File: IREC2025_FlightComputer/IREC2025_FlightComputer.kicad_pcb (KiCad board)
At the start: 2 copper layers, 149 parts, among them J1 Molex Microfit, Q1 SI7232DN-T1-GE3, Q2 SI7232DN-T1-GE3, U1 STM32U575VGTx, U10 PE4259-63, U11 SX1262IMLTRT, U12 ADXL375BCCZ-RL7, U13 MMC5983MA, U14 BMI088, U15 TMP275AIDGKR VSSOP8, U16 MS5607-02BA, U17 KLM4G1FETE-B041, U18 SAM-M10Q-00B, U2 NRVB120VLSFT1G, U4 NRVB120VLSFT1G, U5 LP5912Q3.3DRVRQ1, U8 TPS62153, U9 SN74HCT125DR, X1 1XXD32000MBA, X2 1XXD32000MBA

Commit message: Updated 22/3/2025
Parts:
- added C22: 100nF, PCM_JLCPCB:C_0402, F.Cu at (145.9, 123.5)
- added J2: BOOT0, Connector_PinHeader_2.54mm:PinHeader_1x03_P2.54mm_Vertical, F.Cu at (96.3, 105.8)
- added J3: SWD, Connector_PinHeader_2.54mm:PinHeader_1x04_P2.54mm_Vertical, F.Cu at (142.2, 124.9)
- added R9: 10kΩ, PCM_JLCPCB:R_0402, F.Cu at (145.9, 126.5)
- moved D2 40.2 mm to (131.9, 87.4)
- moved C23 39.7 mm to (124.6, 111.0)
- moved U8 33.1 mm to (126.8, 87.9)
- moved X1 31.6 mm to (131.5, 108.6)
- moved FB1 31.2 mm to (132.5, 99.8)
- moved L1 31.2 mm to (132.5, 102.6)
- moved R8 21.7 mm to (131.8, 76.7)
- moved C20 21.7 mm to (131.6, 79.3)
- moved D4 21.7 mm to (131.9, 73.7)
- moved C27 21.5 mm to (132.4, 105.5)
- moved U4 21.4 mm to (101.4, 107.9)
- moved U2 21.4 mm to (101.4, 104.9)
- moved D3 21.2 mm to (127.7, 83.2)
- moved U14 20.2 mm to (132.5, 119.8)
- moved R20 20.2 mm to (124.0, 117.9)
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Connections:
- U1 pad 12: unconnected-(U1-PH0-Pad12) -> HSE_IN
- U1 pad 14: NRST -> /NRST
- U1 pad 70: unconnected-(U1-PA11-Pad70) -> USB_DN
- U1 pad 71: MS5607_CS -> USB_DP
- U1 pad 72: unconnected-(U1-PA13-Pad72) -> SWDIO
- U1 pad 76: unconnected-(U1-PA14-Pad76) -> SWCLK
- U1 pad 77: unconnected-(U1-PA15-Pad77) -> MS5607_NSS
- U1 pad 81: BMI_accel_INT1 -> BMI_GYRO_CS
- U1 pad 82: BMI_GYRO_INT1 -> BMI_accel_CS
- U1 pad 83: unconnected-(U1-PD2-Pad83) -> BMI_accel_INT1
- U1 pad 84: unconnected-(U1-PD3-Pad84) -> BMI_GYRO_INT1
- U1 pad 94: unconnected-(U1-PH3-Pad94) -> /BOOT0
- U16 pad 4: MS5607_CS -> MS5607_NSS
- U16 pad 5: MS5607_CS -> MS5607_NSS
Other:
- copper layers 2 -> 4

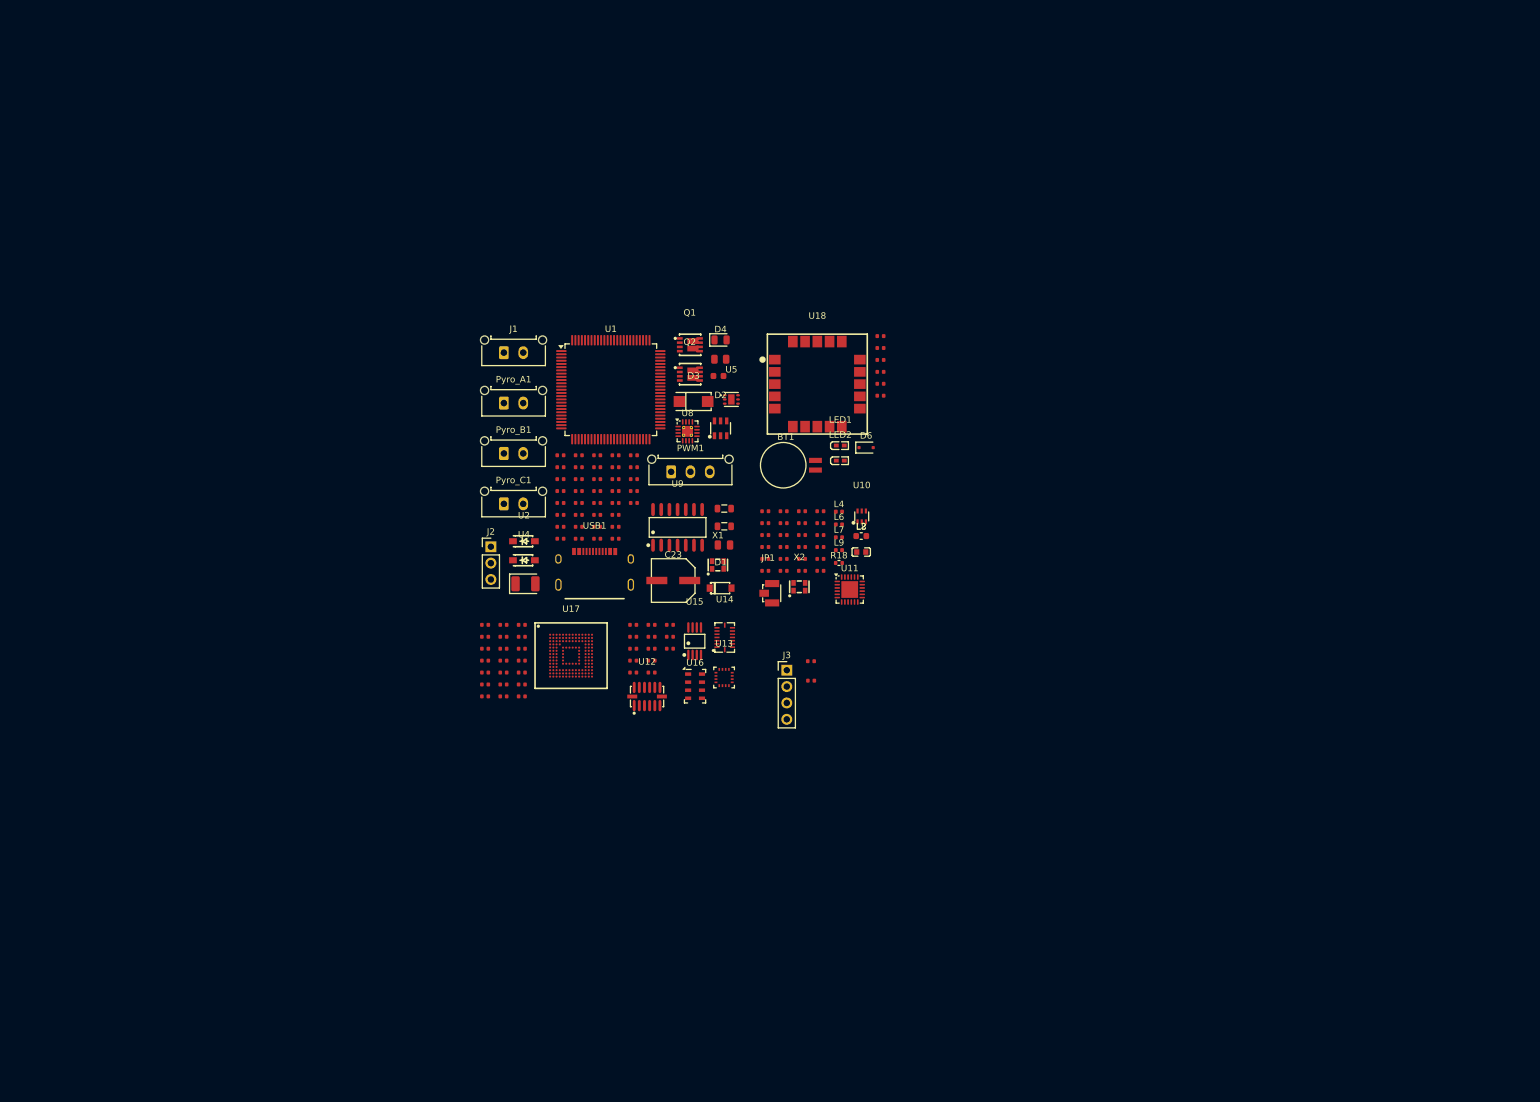
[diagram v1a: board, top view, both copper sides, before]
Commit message: Updated schematic + initiate layout
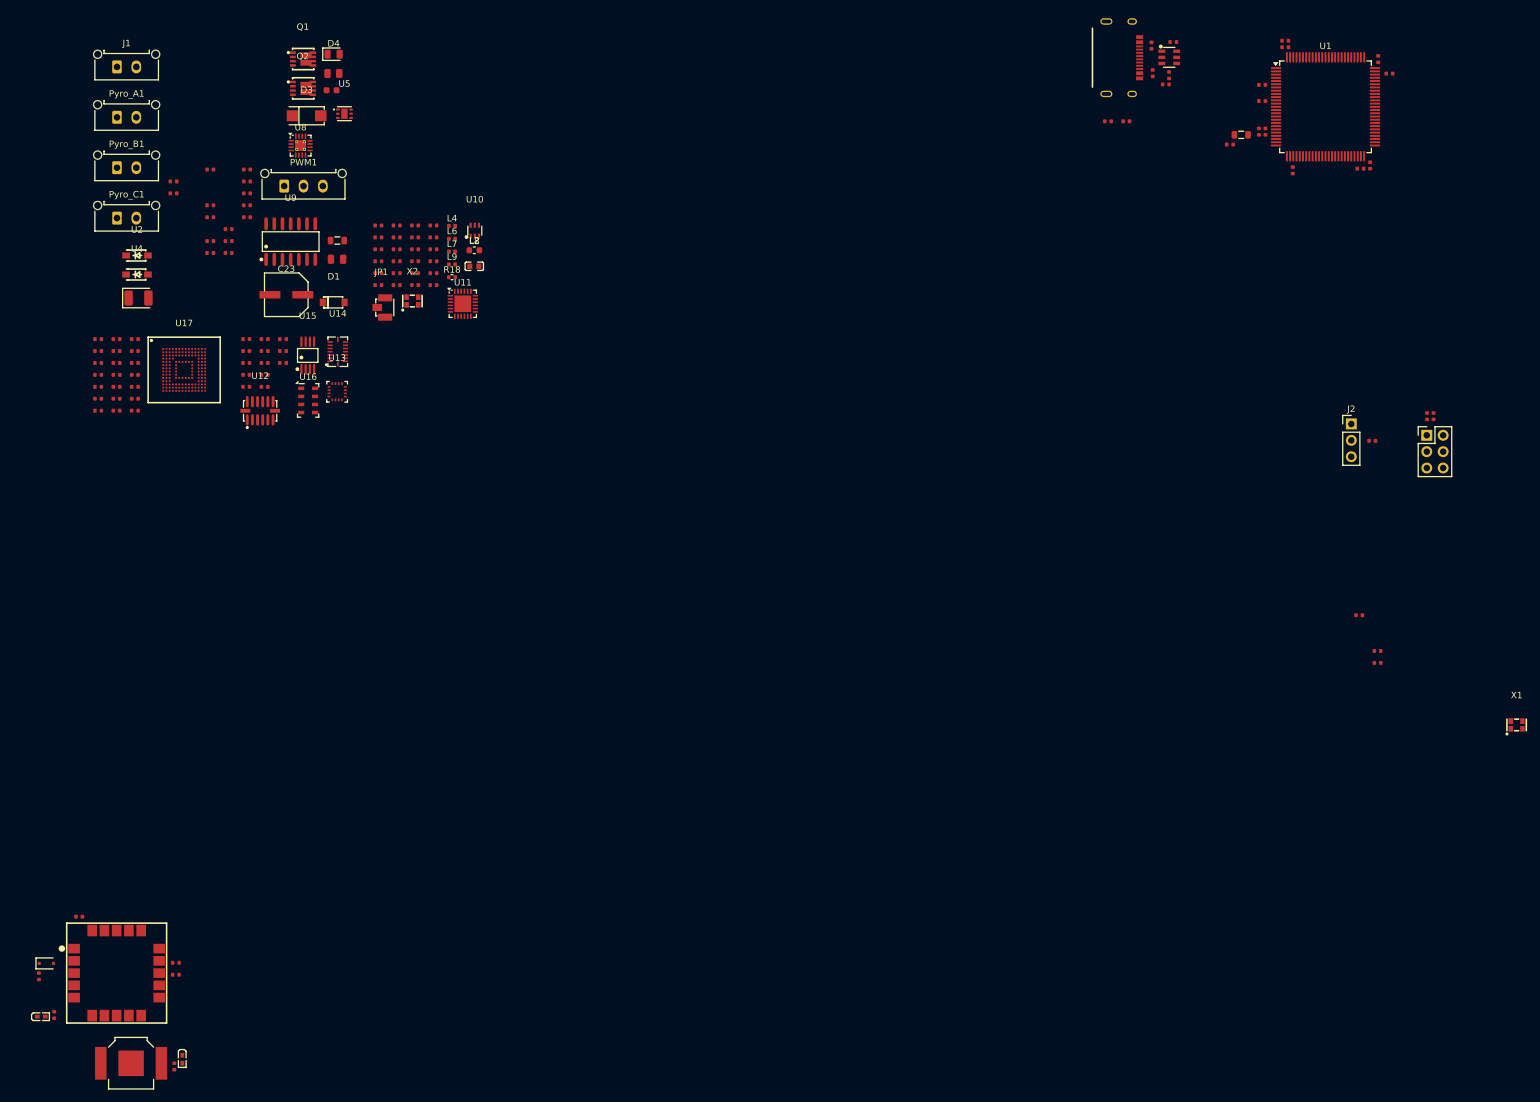
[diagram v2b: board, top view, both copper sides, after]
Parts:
- removed J3: SWD, Connector_PinHeader_2.54mm:PinHeader_1x04_P2.54mm_Vertical
- added J4: Conn_02x03_Counter_Clockwise, Connector_PinHeader_2.54mm:PinHeader_2x03_P2.54mm_Vertical, F.Cu at (241.5, 88.5)
- added R38: 10kΩ, PCM_JLCPCB:R_0402, F.Cu at (241.5, 85.5)
- BT1: value Battery -> 3098; footprint Battery:BatteryHolder_Seiko_MS621F -> GNSS:BAT_3098
- moved R35 162.4 mm to (28.5, 178.4), turned to -90 degrees
- moved R37 158.6 mm to (26.1, 172.4), turned to -90 degrees
- moved C71 153.5 mm to (32.4, 163.2)
- moved R36 152.4 mm to (47.1, 186.4), turned to -90 degrees
- moved LED1 152.4 mm to (26.5, 178.7)
- moved D6 150.3 mm to (27.3, 170.4)
- moved C8 147.5 mm to (235.7, 32.4)
- moved C6 145.2 mm to (233.9, 30.1), turned to 90 degrees
- moved R33 145.1 mm to (47.4, 170.3)
- moved R34 145.1 mm to (47.4, 172.2)
- moved U18 142.0 mm to (38.2, 171.9)
- moved BT1 141.0 mm to (40.4, 185.9)
- moved LED2 138.0 mm to (48.4, 185.3), turned to -90 degrees
- moved C5 136.1 mm to (232.7, 46.6), turned to -90 degrees
- moved C7 134.8 mm to (219.5, 28.2)
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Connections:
- net /BOOT0 renamed Net-(U1-PH3)
- net /NRST renamed nRST
- net Net-(J2-Pin_2) renamed BOOT0
- C14 pad 1: Net-(C14-Pad1) -> +3.3VA
- C15 pad 1: Net-(C14-Pad1) -> +3.3VA
- C16 pad 1: +3.3VA -> +3.3V
- D2 pad 1: D- -> D+
- D2 pad 3: USB_DN -> D-
- D2 pad 4: USB_DP -> USB_DN
- D2 pad 6: D+ -> USB_DP
- FB1 pad 1: Net-(C14-Pad1) -> +3.3VA
- FB1 pad 2: +3.3VA -> +3.3V
- R36 pad 1: +3V3 -> Net-(LED2-+)
- R36 pad 2: Net-(LED2-+) -> Backup
- U1 pad 16: unconnected-(U1-PC1-Pad16) -> eMMC_CLK
- U1 pad 33: unconnected-(U1-PC4-Pad33) -> COMPANION_TX
- U1 pad 34: unconnected-(U1-PC5-Pad34) -> COMPANION_RX
- U1 pad 51: ADXL_NSS -> unconnected-(U1-PB12-Pad51)
- U1 pad 52: ADXL_SCLK -> unconnected-(U1-PB13-Pad52)
- U1 pad 53: ADXL_MISO -> DAT1
- U1 pad 54: ADXL_MOSI -> DAT0
- U1 pad 63: unconnected-(U1-PC6-Pad63) -> DAT7
- U1 pad 64: unconnected-(U1-PC7-Pad64) -> DAT6
- U1 pad 88: unconnected-(U1-PD7-Pad88) -> eMMC_CMD
- U1 pad 89: unconnected-(U1-PB3-Pad89) -> DAT2
- U1 pad 90: unconnected-(U1-PB4-Pad90) -> DAT3
- U1 pad 95: unconnected-(U1-PB8-Pad95) -> DAT4
- U1 pad 96: unconnected-(U1-PB9-Pad96) -> DAT5

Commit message: update idk
25/3/2025
starting to take shape (i guess)
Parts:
- C57, C58, C59, R19, R20, R21, R22: moved to B.Cu
- D3: footprint EasyEDA:SMA_L4.4-W2.6-LS5.0-RD -> GNSS:DIOM7959X262N
- L1: footprint PCM_JLCPCB:L_0805 -> EasyEDA:IND-SMD_L4.0-W4.0_XFL4020-102MEB
- moved R2 152.5 mm to (203.6, 38.2)
- moved C17 151.1 mm to (203.6, 39.4)
- moved C55 150.0 mm to (207.3, 63.6)
- moved C54 149.3 mm to (207.2, 68.5)
- moved C25 148.9 mm to (200.8, 38.7)
- moved U2 148.1 mm to (188.6, 44.1)
- moved R1 147.9 mm to (199.0, 36.9)
- moved R10 146.0 mm to (201.0, 43.4), turned to 90 degrees
- moved R19 143.9 mm to (204.3, 66.1), turned to 90 degrees
- moved C59 143.6 mm to (202.1, 51.8), turned to 90 degrees
- moved J1 143.5 mm to (181.7, 32.6), turned to 180 degrees
- moved U4 142.5 mm to (182.6, 44.1), turned to 180 degrees
- moved R20 141.9 mm to (205.8, 69.0), turned to 90 degrees
- moved C57 139.0 mm to (197.9, 50.9)
- moved C58 138.7 mm to (198.2, 55.9), turned to -90 degrees
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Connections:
- U1 pad 33: COMPANION_TX -> COMPANION_RX
- U1 pad 34: COMPANION_RX -> COMPANION_TX
- U1 pad 59: unconnected-(U1-PD12-Pad59) -> MMC_SCL
- U1 pad 60: unconnected-(U1-PD13-Pad60) -> MMC_SDA
- U1 pad 78: SPI3_SCLK -> BMI_SCLK
- U1 pad 79: SPI3_MISO -> BMI_MISO
- U1 pad 80: SPI3_MOSI -> BMI_MOSI
- U1 pad 82: BMI_accel_CS -> unconnected-(U1-PD1-Pad82)
- U1 pad 83: BMI_accel_INT1 -> unconnected-(U1-PD2-Pad83)
- U1 pad 85: unconnected-(U1-PD4-Pad85) -> BMI_GYRO_INT2
- U1 pad 86: unconnected-(U1-PD5-Pad86) -> BMI_accel_CS
- U1 pad 87: unconnected-(U1-PD6-Pad87) -> BMI_accel_INT1
- U1 pad 92: unconnected-(U1-PB6-Pad92) -> TMP_SCL
- U1 pad 93: unconnected-(U1-PB7-Pad93) -> TMP_SDA
- U12 pad 1: VBAT- -> +3.3V
- U16 pad 6: MS5607_MISO -> BMI_MISO
- U16 pad 7: MS5607_MOSI -> BMI_MOSI
- U16 pad 8: MS5607_SCLK -> BMI_SCLK
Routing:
- net BMI_MISO: track 0.00 -> 18.5 mm, vias 0 -> 3
- net BMI_SCLK: track 0.00 -> 11.6 mm
- net BMI_accel_INT1: track 0.00 -> 5.97 mm
- net BMI_accel_CS: track 0.00 -> 4.94 mm
- net BMI_GYRO_INT2: track 0.00 -> 4.94 mm
- net BMI_GYRO_INT1: track 0.00 -> 4.94 mm
- net BMI_MOSI: track 0.00 -> 4.73 mm
- net TMP_SCL: track 0.00 -> 3.57 mm, vias 0 -> 1
- net TMP_SDA: track 0.00 -> 3.54 mm, vias 0 -> 1
- net MS5607_NSS: track 0.00 -> 2.15 mm
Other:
- board text added: "ADXL"
- board text added: "GNSS"

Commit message: checkpoint
before the great layout change
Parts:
- removed C19: 100nF, PCM_JLCPCB:C_0402
- removed C29: 3.0pF, PCM_JLCPCB:C_0402
- removed C33, C36, C40, C42: C_Small, PCM_JLCPCB:C_0402
- removed C44: 1uF, PCM_JLCPCB:C_0402
- removed C62, C63, C64, C65, C66, C67, C68, C69: 10nF, PCM_JLCPCB:C_0402
- removed D4: 3v3_led, LED_SMD:LED_0805_2012Metric
- removed JP1: U.FL-R-SMT-1(10), EasyEDA:ANT-SMD_UFL-R-SMT-1-10
- removed L8: 15nH, Inductor_SMD:L_0603_1608Metric
- removed Pyro_C1: Molex Microfit, Connector_Molex:Molex_Micro-Fit_3.0_43650-0215_1x02_P3.00mm_Vertical
- removed Q2: SI7232DN-T1-GE3, EasyEDA:POWER-1212-8_L3.3-W3.3-P0.66-LS3.3-BL
- removed R18: 1k, Resistor_SMD:R_0402_1005Metric
- removed R25, R26, R27, R28, R29, R30, R32, R7: 22kΩ, PCM_JLCPCB:R_0402
- removed R31: 47kΩ, PCM_JLCPCB:R_0402
- removed R5: 1MΩ, PCM_JLCPCB:R_0402
- removed R6: 10kΩ, PCM_JLCPCB:R_0402
- removed R8: 1kΩ, PCM_JLCPCB:R_0805
- removed U17: KLM4G1FETE-B041, EasyEDA:FBGA-153_L11.0-W10.0-P0.50_KLM4G1FETE-B041
- added BZ1: PKMCS0909E4000-R1, Buzzer_Beeper:PUIAudio_SMT_0825_S_4_R, F.Cu at (84.7, 91.5)
- added C24: 10uF, PCM_JLCPCB:C_0805, F.Cu at (90.4, 138.6)
- added C73: 10uF, PCM_JLCPCB:C_0402, F.Cu at (72.4, 95.2)
- added C74: 100uF, EasyEDA:CAP-SMD_L3.2-W1.6, F.Cu at (107.1, 123.2)
- added H1: MountingHole_Pad, MountingHole:MountingHole_3.2mm_M3_DIN965_Pad, F.Cu at (120.9, 139.0)
- added H2: MountingHole_Pad, MountingHole:MountingHole_3.2mm_M3_DIN965_Pad, F.Cu at (54.6, 139.2)
- added H3: MountingHole_Pad, MountingHole:MountingHole_3.2mm_M3_DIN965_Pad, F.Cu at (141.3, 54.2)
- added H4: MountingHole_Pad, MountingHole:MountingHole_3.2mm_M3_DIN965_Pad, F.Cu at (33.3, 62.9)
- added LOGO: LOGO, Cuharlogo:CUHARLOGOMOD, F.Cu at (29.5, 88.6)
- added R49: 22kΩ, PCM_JLCPCB:R_0402, B.Cu at (97.2, 113.3)
- added R50: 22kΩ, PCM_JLCPCB:R_0402, B.Cu at (93.8, 105.0)
- added R51: 22kΩ, PCM_JLCPCB:R_0402, F.Cu at (84.7, 102.3)
- added R52: 22kΩ, PCM_JLCPCB:R_0402, B.Cu at (96.0, 102.7)
- added R53: 22kΩ, PCM_JLCPCB:R_0402, F.Cu at (81.1, 102.9)
- added R54: 22kΩ, PCM_JLCPCB:R_0402, F.Cu at (78.5, 105.9)
- added R55: 22kΩ, PCM_JLCPCB:R_0402, F.Cu at (76.0, 102.3)
- added R56: 22kΩ, PCM_JLCPCB:R_0402, F.Cu at (76.0, 105.7)
- added R57: 22kΩ, PCM_JLCPCB:R_0402, F.Cu at (69.7, 95.6)
- added R58: 47kΩ, PCM_JLCPCB:R_0402, F.Cu at (71.2, 109.8)
- added RF1: SMA-KE-5, EasyEDA:SMA-TH_SMA-KHDB_C9900020423, F.Cu at (61.9, 71.3)
- added SERVO2: Conn_01x03_Pin, Connector_Molex:Molex_Micro-Fit_3.0_43650-0315_1x03_P3.00mm_Vertical, F.Cu at (55.6, 121.0)
- added U6: ~, RFshielddd:MS233-20, F.Cu at (79.1, 69.9)
- added U7: THGBMUG6C1LBAIL, EasyEDA:BGA-153_L13.0-W11.5-P0.50-TL_KLM8G1GEME-B041, F.Cu at (67.5, 101.6)
- C11, C34, C35, C43, C45, C51, C52, C53, R9: moved to B.Cu
- C20: footprint PCM_JLCPCB:C_0603 -> PCM_JLCPCB:C_0805; moved to B.Cu
- C21: footprint PCM_JLCPCB:C_0402 -> PCM_JLCPCB:C_0603
- C23: value RVT1E101M0607 -> 22uF; footprint EasyEDA:CAP-SMD_BD6.3-L6.6-W6.6-LS7.2-R-RD -> PCM_JLCPCB:C_0603; moved to B.Cu
- C25: value 3.3pF -> GJM1555C1H3R3BB01D; footprint PCM_JLCPCB:C_0402 -> EasyEDA:C0402
- C26: footprint PCM_JLCPCB:C_0402 -> PCM_JLCPCB:C_0603; moved to B.Cu
- C27: value 22uF -> GJM1555C1H390JB01D; footprint PCM_JLCPCB:C_0805 -> PCM_JLCPCB:C_0402
- C28: footprint PCM_JLCPCB:C_CASE-B-3528-21(mm) -> EasyEDA:CAP-SMD_L3.2-W1.6
- C37: value C_Small -> 3pF
- C38: value C_Small -> 5.6pF
- C39: value C_Small -> 2.4pF
- C4: footprint PCM_JLCPCB:C_0402 -> PCM_JLCPCB:C_0805
- C41: value 10nF -> 39pF
- C46, C47: value C_Small -> GJM1555C1H3R3BB01D; footprint PCM_JLCPCB:C_0402 -> EasyEDA:C0402
- C48: value C_Small -> GRM155R72A102KA01D; footprint PCM_JLCPCB:C_0402 -> EasyEDA:C0402
- C49: value 10nF -> 1uF; moved to B.Cu
- C50: value 1nF -> GRM155R72A102KA01D; footprint PCM_JLCPCB:C_0402 -> EasyEDA:C0402
- C60: value 10uF -> 1.8pF
- C61: value 10nF -> 1.8pF
- C70: value 10uF -> 100nF
- L3: value 47nH -> 15uH; footprint PCM_JLCPCB:C_0402 -> EasyEDA:L0805; moved to B.Cu
- L4: value 0R -> 47nH; footprint Inductor_SMD:L_0402_1005Metric -> PCM_JLCPCB:L_0402
- L6: value L_Small -> 4.7nH
- L7: value L_Small -> 15nH
- L9: value L_Small -> LQW15AN9N1H00D
- R11: value 3.3kΩ -> 0R
- R23, R24: value 22kΩ -> CRCW0402100RFKED
- moved BT1 159.1 mm to (108.6, 42.1), turned to 180 degrees
- moved R36 154.8 mm to (101.9, 41.6), turned to 90 degrees
- moved LED2 151.8 mm to (100.7, 42.7), turned to 90 degrees
- moved R2 150.9 mm to (87.0, 134.0), turned to 180 degrees
- moved C17 149.3 mm to (87.0, 132.7), turned to 180 degrees
- moved X1 147.8 mm to (109.8, 107.9), turned to 180 degrees
- moved D1 147.7 mm to (85.9, 130.4), turned to 0 degrees
- moved C25 145.7 mm to (90.0, 133.4)
- moved R1 145.3 mm to (91.6, 134.7), turned to 180 degrees
- moved R37 145.3 mm to (104.2, 49.9), turned to 180 degrees
- moved D6 143.1 mm to (106.2, 51.0), turned to -90 degrees
- moved D3 141.4 mm to (98.4, 137.7), turned to 0 degrees
- moved R10 140.4 mm to (89.5, 128.6), turned to -90 degrees
- moved U8 138.3 mm to (93.5, 131.8), turned to -90 degrees
- moved LED1 137.4 mm to (94.1, 59.0), turned to 180 degrees
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- renumbered Pyro_A1 to Pyro_CH1, Pyro_B1 to Pyro_CH2, PWM1 to SERVO1
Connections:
- C23 pad 1: Net-(U2-K) -> VBAT-
- C23 pad 2: VBAT- -> +5V
- C25 pad 1: Net-(U8-SS/TR) -> VBAT-
- C25 pad 2: VBAT- -> Net-(U8-SS/TR)
- C27 pad 1: VBAT- -> Net-(U10-RFC)
- C27 pad 2: +5V -> Net-(C27-Pad2)
- C28 pad 1: +3.3V -> +5V
- C3 pad 1: VREF+ -> +3.3VA
- C37 pad 1: Net-(C29-Pad1) -> Net-(C37-Pad1)
- C37 pad 2: VBAT- -> Net-(C37-Pad2)
- C38 pad 1: Net-(C29-Pad2) -> Net-(C37-Pad2)
- C41 pad 1: VBAT- -> Net-(C37-Pad2)
- C41 pad 2: +3.3V -> Net-(C41-Pad2)
- C46 pad 1: Net-(C46-Pad1) -> VBAT-
- C46 pad 2: Net-(U10-RFC) -> Net-(C27-Pad2)
- C47 pad 2: Net-(C46-Pad1) -> Net-(C47-Pad2)
- C48 pad 2: Net-(JP1-SIN) -> Net-(U10-CTRL#orVDD)
- C60 pad 1: +3V3 -> RF1
- C61 pad 1: +3V3 -> Net-(U11-RFI_P)
- C70 pad 1: Net-(U17-VDDI) -> VBAT+
- D6 pad 2: +3V3 -> +3.3V
- J2 pad 1: +3V3 -> +3.3V
- L3 pad 1: Net-(C29-Pad1) -> Net-(U11-VREG)
- L3 pad 2: Net-(U11-VR_PA) -> Net-(U11-DCC_SW)
- L4 pad 1: Net-(U11-RFO) -> Net-(C37-Pad1)
- L4 pad 2: Net-(C29-Pad1) -> Net-(U11-VR_PA)
- L5 pad 1: Net-(C29-Pad1) -> Net-(C37-Pad1)
- L5 pad 2: Net-(C29-Pad2) -> Net-(C37-Pad2)
- L6 pad 1: Net-(C33-Pad2) -> Net-(C41-Pad2)
- L9 pad 1: Net-(C46-Pad1) -> Net-(C27-Pad2)
- L9 pad 2: Net-(JP1-SIN) -> Net-(C47-Pad2)
- R11 pad 1: PYRO_C -> Net-(U11-RFO)
- R11 pad 2: VBAT- -> Net-(C37-Pad1)
- R23 pad 1: +3V3 -> ANT_SW
- R23 pad 2: DAT0 -> Net-(U10-CTRL#orVDD)
- R24 pad 1: +3V3 -> DIO2
- R24 pad 2: DAT1 -> Net-(U10-CTRL)
- R38 pad 1: +3V3 -> +3.3V
- U1 pad 17: unconnected-(U1-PC2-Pad17) -> ADXL_MISO
- U1 pad 18: unconnected-(U1-PC3-Pad18) -> ADXL_MOSI
- U1 pad 2: unconnected-(U1-PE3-Pad2) -> PWM_A
- U1 pad 21: VREF+ -> +3.3VA
- U1 pad 3: unconnected-(U1-PE4-Pad3) -> PWM_B
- U1 pad 4: unconnected-(U1-PE5-Pad4) -> PWM_C
- U1 pad 40: unconnected-(U1-PE9-Pad40) -> BUZZER
- U1 pad 41: unconnected-(U1-PE10-Pad41) -> ADXL_INT2
- U1 pad 42: unconnected-(U1-PE11-Pad42) -> ADXL_INT1
- U1 pad 43: unconnected-(U1-PE12-Pad43) -> LoRa_RST
- U1 pad 44: unconnected-(U1-PE13-Pad44) -> GNSS_SAFEBOOT
- U1 pad 47: unconnected-(U1-PB10-Pad47) -> ADXL_SCLK
- U1 pad 5: unconnected-(U1-PE6-Pad5) -> PWM_D
- U1 pad 51: unconnected-(U1-PB12-Pad51) -> ADXL_NSS
- U1 pad 52: unconnected-(U1-PB13-Pad52) -> BUSY
- U1 pad 53: DAT1 -> DAT0
- U1 pad 54: DAT0 -> DAT1
- U1 pad 55: unconnected-(U1-PD8-Pad55) -> LORA_DIO3
- U1 pad 58: unconnected-(U1-PD11-Pad58) -> RST_n
- U1 pad 63: DAT7 -> DAT6
- U1 pad 64: DAT6 -> DAT7
- U1 pad 69: unconnected-(U1-PA10-Pad69) -> ANT_SW
- U1 pad 83: unconnected-(U1-PD2-Pad83) -> BMI_GYRO_INT1
- U1 pad 84: BMI_GYRO_INT1 -> BMI_GYRO_INT2
- U1 pad 85: BMI_GYRO_INT2 -> BMI_accel_CS
- U1 pad 86: BMI_accel_CS -> BMI_accel_INT1
- U1 pad 87: BMI_accel_INT1 -> BMI_accel_INT2
- U1 pad 91: unconnected-(U1-PB5-Pad91) -> TMP_ALERT
- U1 pad 97: unconnected-(U1-PE0-Pad97) -> BAT_LEVEL
- U10 pad 6: +3.3V -> Net-(U10-CTRL#orVDD)
- U11 pad 15: LORA_RST -> LoRa_RST
- U11 pad 6: DIO3 -> LORA_DIO3
- U14 pad 6: unconnected-(U14-GNDIO-Pad6) -> VBAT-
- U18 pad 17: +3V3 -> +3.3V
- U18 pad 2: +3V3 -> +3.3V
- U9 pad 11: SERVO_A -> SERVO_B
- U9 pad 14: +3.3V -> +5V
- U9 pad 8: PYRO_C -> SERVO_A
- USB1 pad 13: Net-(C19-Pad2) -> VBAT-
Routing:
- net VBAT-: track 0.00 -> 87.0 mm, vias 0 -> 119
- net +3.3V: track 0.00 -> 63.4 mm, vias 0 -> 38
- net +5V: track 0.00 -> 61.9 mm, vias 0 -> 4
- net DAT5: track 0.00 -> 45.2 mm, vias 0 -> 2
- net eMMC_CLK: track 0.00 -> 43.2 mm, vias 0 -> 3
- net ANT_SW: track 0.00 -> 41.8 mm, vias 0 -> 4
- net DAT4: track 0.00 -> 40.7 mm, vias 0 -> 2
- net LoRa_NSS: track 0.00 -> 40.7 mm, vias 0 -> 4
- net SWCLK: track 0.00 -> 40.2 mm, vias 0 -> 2
- net eMMC_CMD: track 0.00 -> 38.7 mm, vias 0 -> 2
- net PWM_D: track 0.00 -> 38.6 mm, vias 0 -> 2
- net LoRa_SCLK: track 0.00 -> 38.4 mm
- net DAT3: track 0.00 -> 38.3 mm, vias 0 -> 4
- net LoRa_MOSI: track 0.00 -> 37.1 mm, vias 0 -> 2
- net SWDIO: track 0.00 -> 36.9 mm, vias 0 -> 2
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- added copper zone on In2.Cu, net +3.3V
- added copper zone on F.Cu, net +3.3VA
- added copper zone on F.Cu, net +5V
- added copper zone on F.Cu, net Net-(J1-Pin_1)
- added copper zone on F.Cu, net Net-(L1-Pad1)
- added copper zone on F.Cu, net Net-(U2-K)
- added copper zone on F.Cu, net VBAT+
- added copper zone on B.Cu, net VBAT-
- added copper zone on F.Cu, net VBAT-
- added copper zone on In1.Cu, net VBAT-
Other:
- board outline added: 72.5 x 105.8 mm
- board text added: "Brm Brm Patapim"
- board text added: "CURSR-IV Flight Computer"
- board text removed: "ADXL"
- board text removed: "GNSS"
